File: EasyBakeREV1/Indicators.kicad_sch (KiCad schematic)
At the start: 13 parts

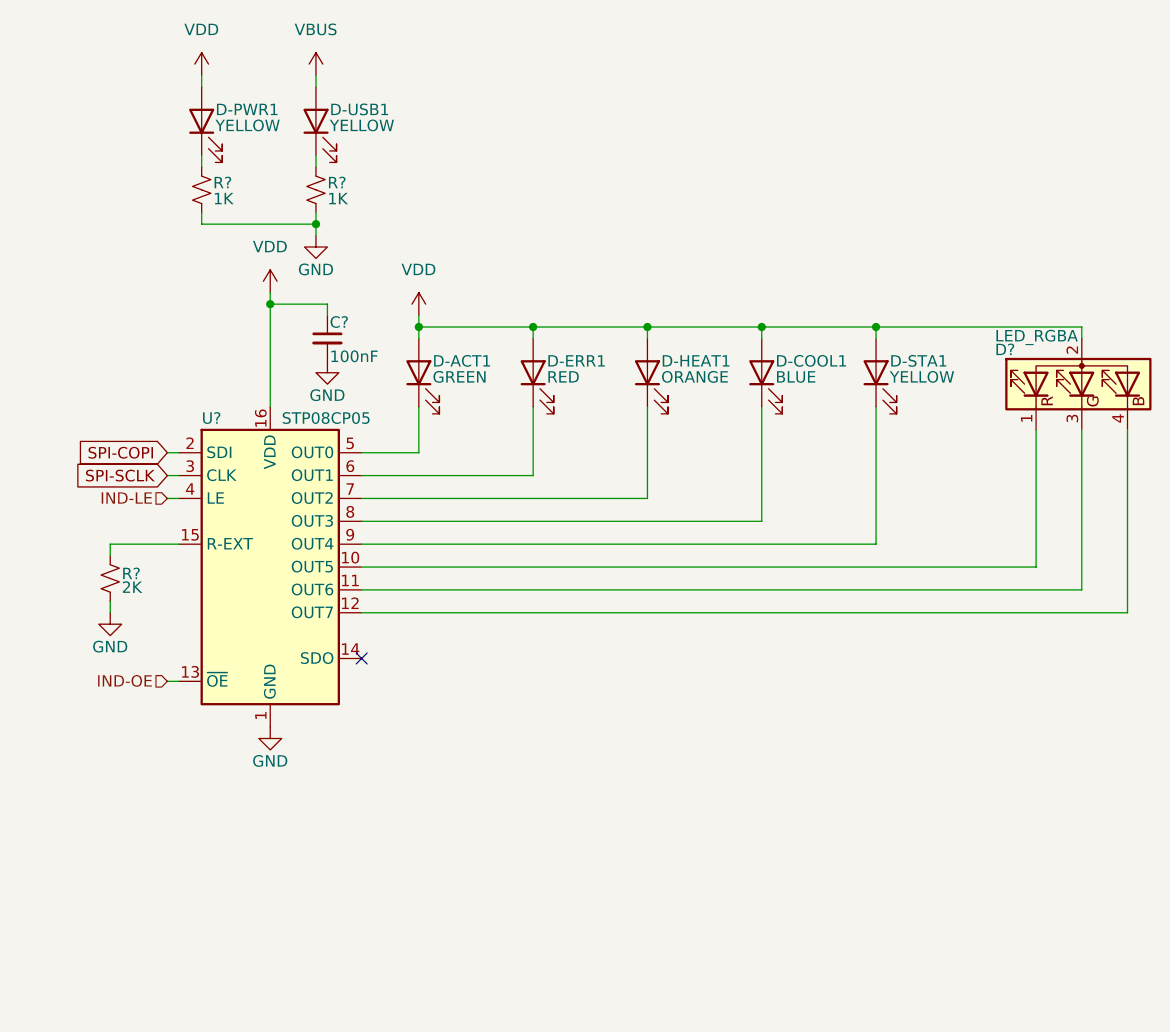
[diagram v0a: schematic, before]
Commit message: REV3 - Reorganize MC pinouts and add LED driver (WIP)
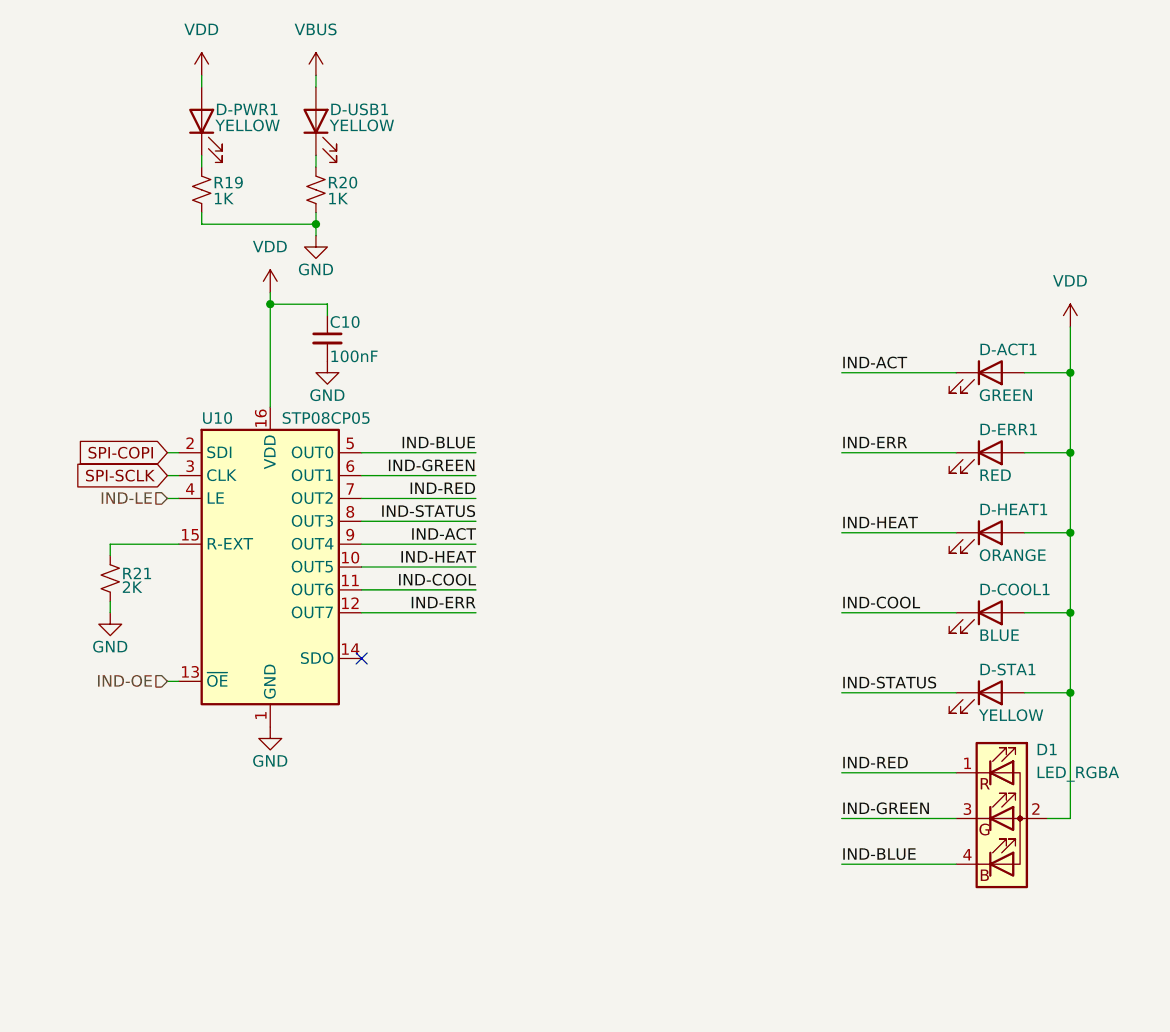
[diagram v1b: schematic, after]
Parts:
- D1: renamed from D?; footprint Daxxn_LEDs:LED_PLCC4_3.2x2.8mm -> Daxxn_LEDs:IN-P32TATRGB
- gave numbers to parts that had none: 5
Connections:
- net IND-HEAT: now reaches U10.10 (OUT5)
- net IND-HEAT: now also D-HEAT1.1 (K); no longer D1.1 (RK)
- net IND-COOL: now reaches U10.11 (OUT6)
- net IND-COOL: now also D-COOL1.1 (K); no longer D1.3 (BK)
- net IND-BLUE: now reaches D1.4 (A)
- net IND-BLUE: now also U10.5 (OUT0); no longer U10.12 (OUT7)
- net IND-ACT: now reaches D-ACT1.1 (K)
- net IND-ACT: now also U10.9 (OUT4); no longer U10.5 (OUT0)
- net IND-ERR: now reaches D-ERR1.1 (K)
- net IND-ERR: now also U10.12 (OUT7); no longer U10.6 (OUT1)
- net IND-RED: now reaches U10.7 (OUT2)
- net IND-RED: now also D1.1 (RK); no longer D-HEAT1.1 (K)
- net IND-STATUS: now reaches U10.8 (OUT3)
- net IND-STATUS: now also D-STA1.1 (K); no longer D-COOL1.1 (K)
- new net IND-GREEN: D1.3 (BK), U10.6 (OUT1)
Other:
- moved on the sheet: D-ACT1, D-COOL1, D-ERR1, D-HEAT1, D-STA1, D1

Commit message: Update to KiCad 7
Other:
- company: (none) -> Daxxn Industries
- title: (none) -> EasyBake Reflow Oven

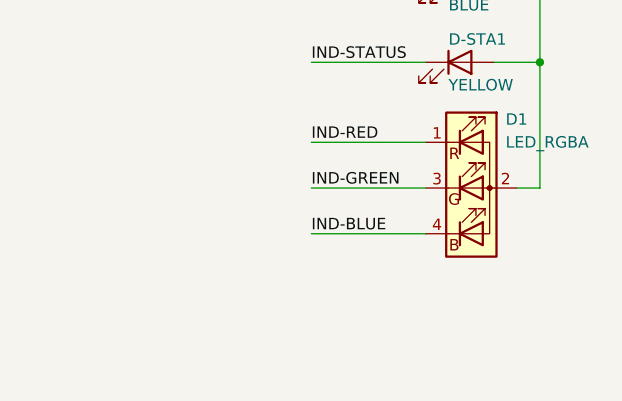
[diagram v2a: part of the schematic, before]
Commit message: NOT programming. Going to rework board...again
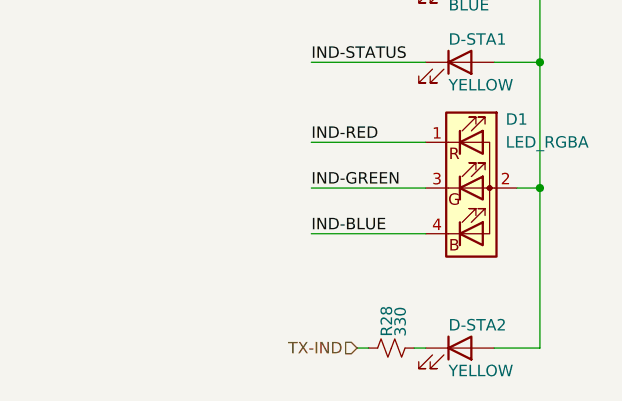
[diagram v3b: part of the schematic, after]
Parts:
- added D-STA2: YELLOW, LED_SMD:LED_0805_2012Metric_Pad1.15x1.40mm_HandSolder, symbol Device:LED
- added R28: 330, Resistor_SMD:R_0603_1608Metric, symbol Device:R_Small_US
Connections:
- net VDD: now also D-STA2.2 (A)
- new net: D-STA2.1 (K), R28.2
- new net TX-IND: R28.1
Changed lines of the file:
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@@
   (junction (at 134.62 93.98) (diameter 0) (color 0 0 0 0)
+  )
+  (junction (at 134.62 107.95) (diameter 0) (color 0 0 0 0)
   )
   (junction (at 134.62 67.31) (diameter 0) (color 0 0 0 0)
@@
     (stroke (width 0) (type default))
   )
+  (wire (pts (xy 120.65 125.73) (xy 121.92 125.73))
+    (stroke (width 0) (type default))
+  )
   (wire (pts (xy 134.62 93.98) (xy 134.62 107.95))
     (stroke (width 0) (type default))
@@
     (stroke (width 0) (type default))
   )
+  (wire (pts (xy 114.3 125.73) (xy 115.57 125.73))
+    (stroke (width 0) (type default))
+  )
   (wire (pts (xy 50.8 25.4) (xy 50.8 26.67))
     (stroke (width 0) (type default))
@@
     (stroke (width 0) (type default))
   )
+  (wire (pts (xy 134.62 107.95) (xy 134.62 125.73))
+    (stroke (width 0) (type default))
+  )
   (wire (pts (xy 134.62 67.31) (xy 134.62 76.2))
     (stroke (width 0) (type default))
@@
   )
   (wire (pts (xy 34.29 92.71) (xy 35.56 92.71))
+    (stroke (width 0) (type default))
+  )
+  (wire (pts (xy 134.62 125.73) (xy 129.54 125.73))
     (stroke (width 0) (type default))
   )
@@
       (effects (font (size 1.27 1.27)) (justify right) hide)
     )
+  )
+  (hierarchical_label "TX-IND" (shape input) (at 114.3 125.73 180) (fields_autoplaced)
+    (effects (font (size 1.27 1.27)) (justify right))
   )
   (hierarchical_label "IND-LE" (shape input) (at 34.29 72.39 180) (fields_autoplaced)
@@
     )
   )
+  (symbol (lib_id "Device:R_Small_US") (at 118.11 125.73 90) (unit 1)
+    (in_bom yes) (on_board yes) (dnp no)
+    (property "Reference" "R28" (at 117.602 124.46 0)
+      (effects (font (size 1.27 1.27)) (justify left))
+    )
+    (property "Value" "330" (at 119.126 124.46 0)
+      (effects (font (size 1.27 1.27)) (justify left))
+    )
+    (property "Footprint" "Resistor_SMD:R_0603_1608Metric" (at 118.11 125.73 0)
+      (effects (font (size 1.27 1.27)) hide)
+    )
+    (property "Datasheet" "~" (at 118.11 125.73 0)
+      (effects (font (size 1.27 1.27)) hide)
+    )
+    (property "Schematic" "" (at 118.11 125.73 0)
+      (effects (font (size 1.27 1.27)) hide)
+    )
+    (property "PartNumber" "" (at 118.11 125.73 0)
+      (effects (font (size 1.27 1.27)))
+    )
+    (property "SupplierPN" "" (at 118.11 125.73 0)
+      (effects (font (size 1.27 1.27)) hide)
+    )
+    (pin "1")
+    (pin "2")
+    (instances
+      (project "EasyBakeREV1"
+        (path "/e63e39d7-6ac0-4ffd-8aa3-1841a4541b55/a9601474-acad-4e52-ad82-40858ef5b30f"
+          (reference "R28") (unit 1)
+        )
+      )
+    )
+  )
   (symbol (lib_id "Daxxn_LEDs:LED_RGBA") (at 127 107.95 0) (unit 1)
     (in_bom yes) (on_board yes) (dnp no)
@@
         )
       )
+    )
+  )
+  (symbol (lib_id "Device:LED") (at 125.73 125.73 0) (unit 1)
+    (in_bom yes) (on_board yes) (dnp no)
+    (property "Reference" "D-STA2" (at 124.46 123.19 0)
+      (effects (font (size 1.27 1.27)) (justify left))
+    )
+    (property "Value" "YELLOW" (at 124.46 128.27 0)
+      (effects (font (size 1.27 1.27)) (justify left))
+    )
+    (property "Footprint" "LED_SMD:LED_0805_2012Metric_Pad1.15x1.40mm_HandSolder" (at 125.73 125.73 0)
+      (effects (font (size 1.27 1.27)) hide)
+    )
+    (property "Datasheet" "~" (at 125.73 125.73 0)
+      (effects (font (size 1.27 1.27)) hide)
+    )
+    (pin "1")
+    (pin "2")
+    (instances
+      (project "EasyBakeREV1"
+        (path "/e63e39d7-6ac0-4ffd-8aa3-1841a4541b55/a9601474-acad-4e52-ad82-40858ef5b30f"
+          (reference "D-STA2") (unit 1)
+        )
+      )
